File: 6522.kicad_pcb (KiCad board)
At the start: 2 copper layers, 65.8 x 81.4 mm, 20 parts, among them J1 Conn_02x20_Top_Bottom, J2 Conn_02x01_Top_Bottom, P1 A2Bus, U1 74LS245, U2 74LS04, U3 74LS74, U4 W65C22, U5 W65C22

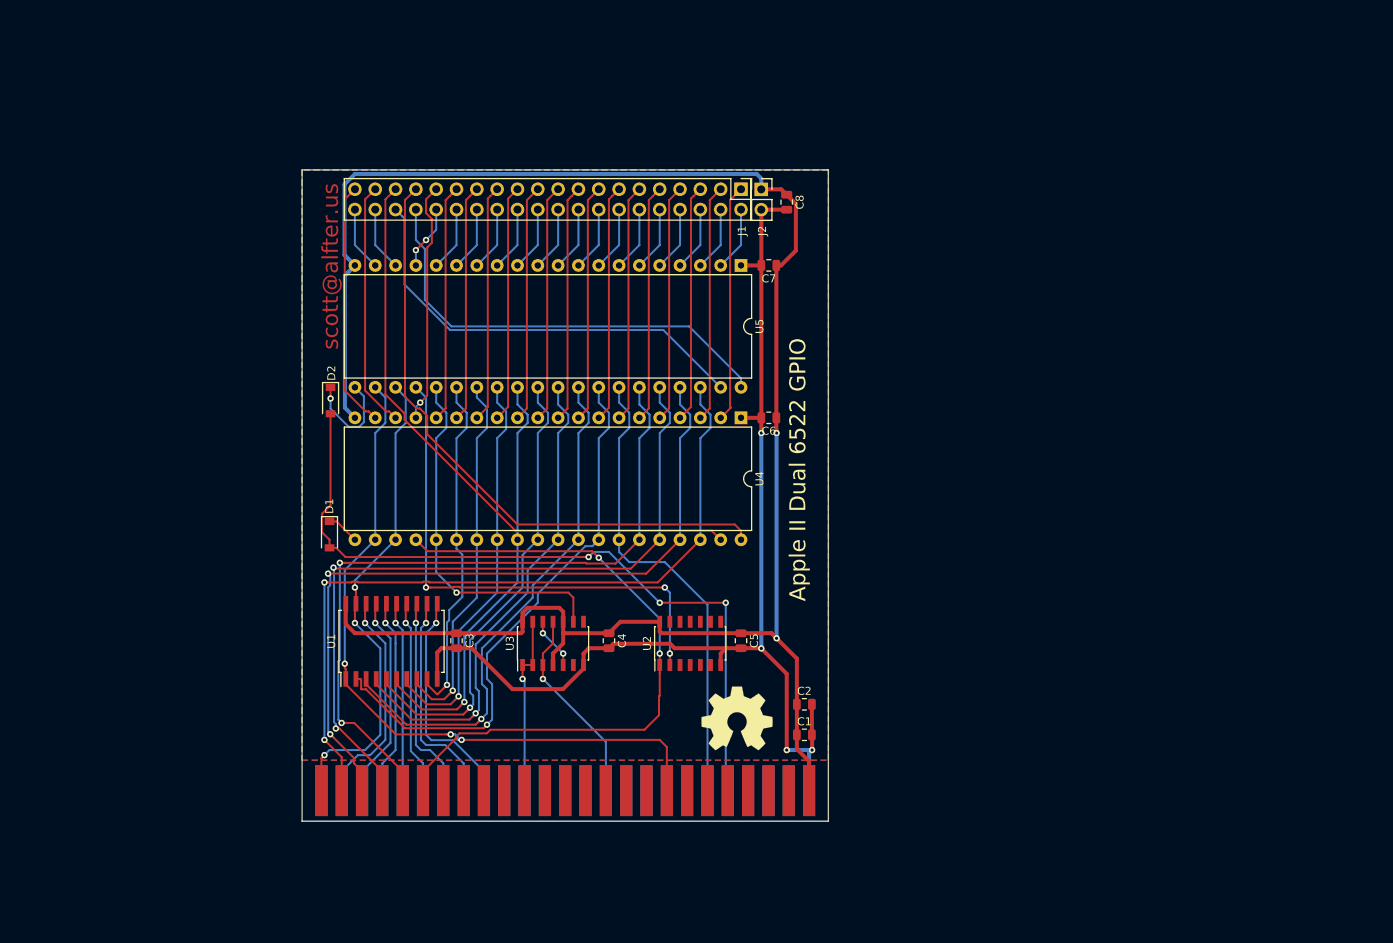
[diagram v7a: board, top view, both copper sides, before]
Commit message: Mockingboard with delay-based Phi2
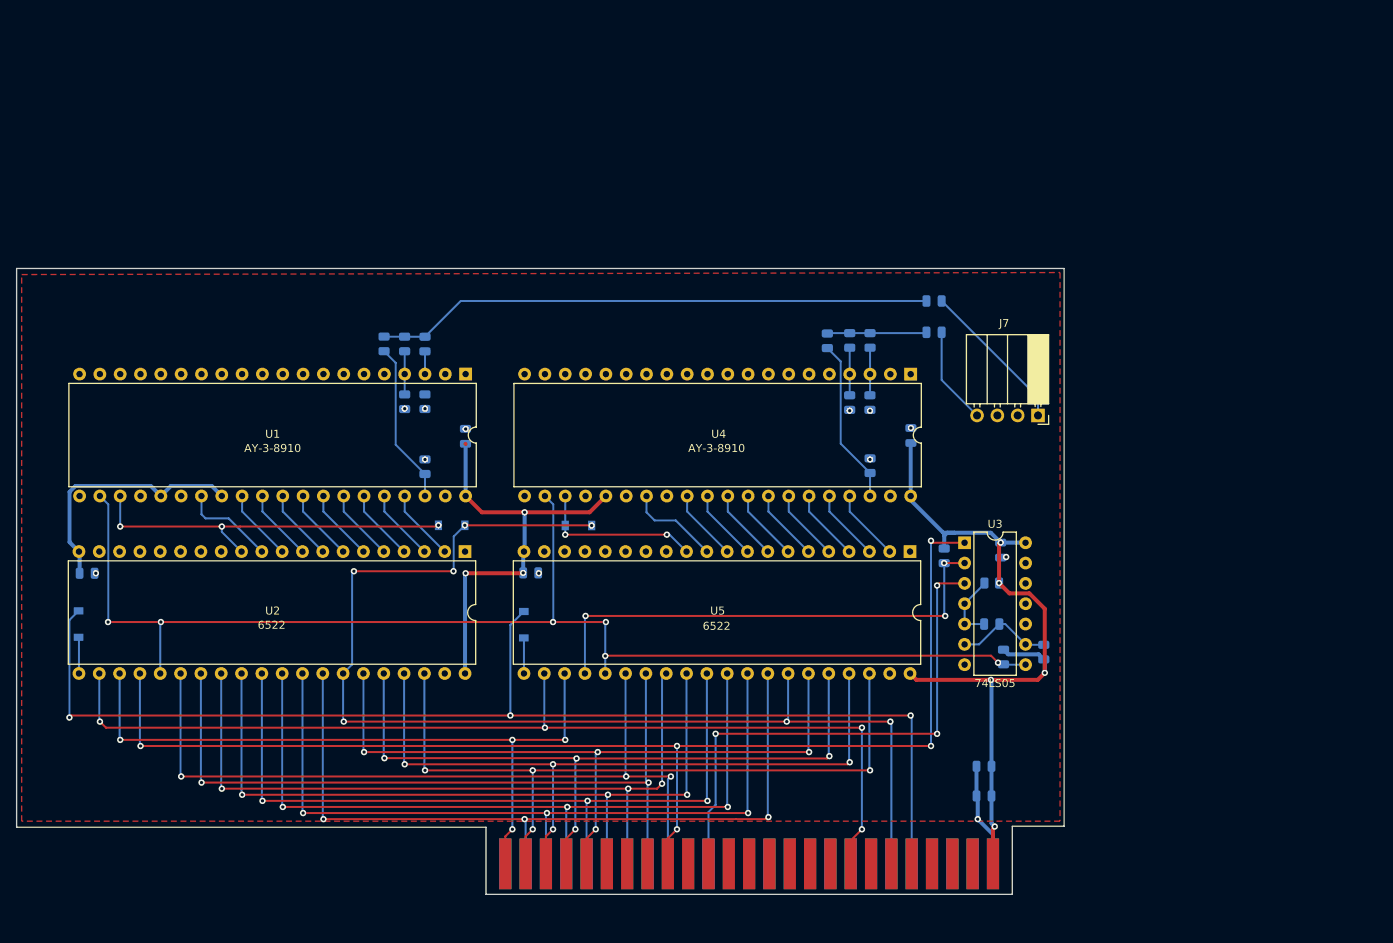
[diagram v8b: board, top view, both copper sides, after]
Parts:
- removed the C8 at (172.0, 56.7)
- removed G***: LOGO, qr:qr
- removed J1: Conn_02x20_Top_Bottom, Connector_PinHeader_2.54mm:PinHeader_2x20_P2.54mm_Vertical
- removed J2: Conn_02x01_Top_Bottom, Connector_PinHeader_2.54mm:PinHeader_2x01_P2.54mm_Vertical
- removed REF**: OSHW-Symbol_8.9x8mm_SilkScreen, Symbol:OSHW-Symbol_8.9x8mm_SilkScreen
- removed the U2 at (159.9, 111.9)
- added C1: 10μF, Capacitor_SMD:C_0805_2012Metric, B.Cu at (190.4, 69.1)
- added C10: 10μF, Capacitor_SMD:C_0805_2012Metric, B.Cu at (190.4, 73.0)
- added C9: 5pF, Capacitor_SMD:C_0805_2012Metric, B.Cu at (197.6, 109.5)
- added D1: BAT54GW, Diode_SMD:D_SOD-123, B.Cu at (130.1, 97.1)
- added D3: BAT54GW, Diode_SMD:D_SOD-123, B.Cu at (145.9, 97.2)
- added J7: AUDIO_OUT, Connector_PinSocket_2.54mm:PinSocket_1x04_P2.54mm_Horizontal, F.Cu at (203.4, 83.4)
- added R1: 1k, Resistor_SMD:R_0805_2012Metric, B.Cu at (124.2, 74.5)
- added R10: 1k0, Resistor_SMD:R_0805_2012Metric, B.Cu at (199.1, 113.6)
- added R11: 1k, Resistor_SMD:R_0805_2012Metric, B.Cu at (179.8, 74.0)
- added R12: 1k, Resistor_SMD:R_0805_2012Metric, B.Cu at (182.4, 74.0)
- added R13: 1k, Resistor_SMD:R_0805_2012Metric, B.Cu at (177.0, 74.1)
- added R14: 470, Resistor_SMD:R_0805_2012Metric, B.Cu at (179.8, 81.8)
- added R15: 470, Resistor_SMD:R_0805_2012Metric, B.Cu at (182.4, 81.8)
- added R16: 470, Resistor_SMD:R_0805_2012Metric, B.Cu at (182.4, 89.7)
- added R2: 1k, Resistor_SMD:R_0805_2012Metric, B.Cu at (126.7, 74.5)
- added R3: 1k, Resistor_SMD:R_0805_2012Metric, B.Cu at (121.6, 74.5)
- added R4: 470, Resistor_SMD:R_0805_2012Metric, B.Cu at (124.2, 81.7)
- added R5: 470, Resistor_SMD:R_0805_2012Metric, B.Cu at (126.7, 81.7)
- added R6: 470, Resistor_SMD:R_0805_2012Metric, B.Cu at (126.7, 89.8)
- added R7: 10k, Resistor_SMD:R_0805_2012Metric, B.Cu at (191.6, 100.9)
- added R8: 4k7, Resistor_SMD:R_0805_2012Metric, B.Cu at (197.6, 104.3)
- added R9: 4k7, Resistor_SMD:R_0805_2012Metric, B.Cu at (204.1, 113.0)
- added U4: AY-3-8910, Package_DIP:DIP-40_W15.24mm, F.Cu at (187.5, 78.2)
- C2: renamed from C1; moved to B.Cu
- C3: renamed from C2; moved to B.Cu
- C4: renamed from C3; moved to B.Cu
- C5: renamed from C4; moved to B.Cu
- C6: renamed from C5; moved to B.Cu
- C7: renamed from C6; moved to B.Cu
- C8: renamed from C7; moved to B.Cu
- D2: renamed from D1; moved to B.Cu
- D4: renamed from D2; moved to B.Cu
- U1: value 74LS245 -> AY-3-8910; footprint Package_SO:SOIC-20W_7.5x12.8mm_P1.27mm -> Package_DIP:DIP-40_W15.24mm
- U2: renamed from U4; value W65C22 -> 6522
- U3: value 74LS74 -> 74LS05; footprint Package_SO:SOIC-14_3.9x8.7mm_P1.27mm -> Package_DIP:DIP-14_W7.62mm
- U5: value W65C22 -> 6522
- moved C6 82.2 mm to (84.5, 103.1), turned to 0 degrees
- moved C8 71.6 mm to (196.6, 131.0)
- moved U3 53.0 mm to (194.2, 99.3), turned to 0 degrees
- moved C5 50.3 mm to (198.7, 100.2)
- moved U5 41.5 mm to (187.4, 100.4)
- moved U2 38.3 mm to (131.7, 100.4)
- moved C7 38.0 mm to (131.8, 86.0), turned to 90 degrees
- moved D4 37.0 mm to (139.1, 109.6), turned to 90 degrees
- moved C3 36.1 mm to (187.5, 85.9), turned to 90 degrees
- moved U1 34.7 mm to (131.8, 78.2), turned to -90 degrees
- moved D2 33.3 mm to (83.4, 109.5), turned to 90 degrees
- moved P1 24.7 mm to (167.3, 139.4)
- moved C2 22.8 mm to (196.6, 127.3), turned to 180 degrees
- moved C4 12.6 mm to (140.0, 103.1), turned to 0 degrees
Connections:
- net ~IRQ renamed ~{IRQ}
- net ~RES renamed ~{RES}
- P1 pad 1: ~IOSEL -> ~{IOSEL}
- P1 pad 10: Net-(P1-Pad10) -> unconnected-(P1-Pad10)
- P1 pad 11: Net-(P1-Pad11) -> unconnected-(P1-Pad11)
- P1 pad 12: Net-(P1-Pad12) -> unconnected-(P1-Pad12)
- P1 pad 13: Net-(P1-Pad13) -> unconnected-(P1-Pad13)
- P1 pad 14: Net-(P1-Pad14) -> unconnected-(P1-Pad14)
- P1 pad 15: Net-(P1-Pad15) -> unconnected-(P1-Pad15)
- P1 pad 16: Net-(P1-Pad16) -> unconnected-(P1-Pad16)
- P1 pad 17: Net-(P1-Pad17) -> unconnected-(P1-Pad17)
- P1 pad 18: R~W -> R~{W}
- P1 pad 19: Net-(P1-Pad19) -> unconnected-(P1-Pad19)
- P1 pad 20: Net-(P1-Pad20) -> unconnected-(P1-Pad20)
- P1 pad 21: Net-(P1-Pad21) -> unconnected-(P1-Pad21)
- P1 pad 22: Net-(P1-Pad22) -> unconnected-(P1-Pad22)
- P1 pad 27: Net-(P1-Pad27) -> Net-(P1-Pad24)
- P1 pad 28: Net-(P1-Pad28) -> Net-(P1-Pad23)
- P1 pad 29: Net-(P1-Pad29) -> unconnected-(P1-Pad29)
- P1 pad 32: Net-(P1-Pad32) -> unconnected-(P1-Pad32)
- P1 pad 33: Net-(P1-Pad33) -> unconnected-(P1-Pad33)
- P1 pad 34: Net-(P1-Pad34) -> unconnected-(P1-Pad34)
- P1 pad 35: Net-(P1-Pad35) -> unconnected-(P1-Pad35)
- P1 pad 36: 7M -> unconnected-(P1-Pad36)
- P1 pad 37: Net-(P1-Pad37) -> unconnected-(P1-Pad37)
- P1 pad 38: Net-(P1-Pad38) -> unconnected-(P1-Pad38)
- P1 pad 39: Net-(P1-Pad39) -> unconnected-(P1-Pad39)
- P1 pad 41: Net-(P1-Pad41) -> unconnected-(P1-Pad41)
- P1 pad 42: Net-(P1-Pad42) -> D7
- P1 pad 43: Net-(P1-Pad43) -> D6
- P1 pad 44: Net-(P1-Pad44) -> D5
- P1 pad 45: Net-(P1-Pad45) -> D4
- P1 pad 46: Net-(P1-Pad46) -> D3
- P1 pad 47: Net-(P1-Pad47) -> D2
- P1 pad 48: Net-(P1-Pad48) -> D1
- P1 pad 49: Net-(P1-Pad49) -> D0
- P1 pad 50: Net-(P1-Pad50) -> unconnected-(P1-Pad50)
- P1 pad 6: A4 -> unconnected-(P1-Pad6)
- P1 pad 7: Net-(P1-Pad7) -> unconnected-(P1-Pad7)
- P1 pad 8: Net-(P1-Pad8) -> unconnected-(P1-Pad8)
- P1 pad 9: Net-(P1-Pad9) -> A7
- U1 pad 1: R~W -> GND
- U1 pad 10: GND -> unconnected-(U1-Pad10)
- U1 pad 11: Net-(P1-Pad42) -> unconnected-(U1-Pad11)
- U1 pad 12: Net-(P1-Pad43) -> unconnected-(U1-Pad12)
- U1 pad 13: Net-(P1-Pad44) -> unconnected-(U1-Pad13)
- U1 pad 14: Net-(P1-Pad45) -> unconnected-(U1-Pad14)
- U1 pad 15: Net-(P1-Pad46) -> unconnected-(U1-Pad15)
- U1 pad 16: Net-(P1-Pad47) -> unconnected-(U1-Pad16)
- U1 pad 17: Net-(P1-Pad48) -> unconnected-(U1-Pad17)
- U1 pad 18: Net-(P1-Pad49) -> unconnected-(U1-Pad18)
- U1 pad 19: ~IOSEL -> unconnected-(U1-Pad19)
- U1 pad 2: D0 -> unconnected-(U1-Pad2)
- U1 pad 20: VCC -> unconnected-(U1-Pad20)
- U1 pad 3: D1 -> Net-(R2-Pad1)
- U1 pad 4: D2 -> Net-(R1-Pad1)
- U1 pad 5: D3 -> unconnected-(U1-Pad5)
- U1 pad 6: D4 -> unconnected-(U1-Pad6)
- U1 pad 7: D5 -> unconnected-(U1-Pad7)
- U1 pad 8: D6 -> unconnected-(U1-Pad8)
- U1 pad 9: D7 -> unconnected-(U1-Pad9)
- U2 pad 13: PB3 -> unconnected-(U2-Pad13)
- U2 pad 14: PB4 -> unconnected-(U2-Pad14)
- U2 pad 15: PB5 -> unconnected-(U2-Pad15)
- U2 pad 16: PB6 -> unconnected-(U2-Pad16)
- U2 pad 17: PB7 -> unconnected-(U2-Pad17)
- U2 pad 18: CB1 -> unconnected-(U2-Pad18)
- U2 pad 19: CB2 -> unconnected-(U2-Pad19)
- U2 pad 2: PA0 -> Net-(U1-Pad37)
- U2 pad 22: R~W -> R~{W}
- U2 pad 23: ~IOSEL -> ~{IOSEL}
- U2 pad 24: A4 -> A7
- U2 pad 3: PA1 -> Net-(U1-Pad36)
- U2 pad 39: CA2 -> unconnected-(U2-Pad39)
- U2 pad 4: PA2 -> Net-(U1-Pad35)
- U2 pad 40: CA1 -> VCC
- U2 pad 5: PA3 -> Net-(U1-Pad34)
- U2 pad 6: PA4 -> Net-(U1-Pad33)
- U2 pad 7: PA5 -> Net-(U1-Pad32)
- U2 pad 8: PA6 -> Net-(U1-Pad31)
- U2 pad 9: PA7 -> Net-(U1-Pad30)
- U3 pad 1: PHI0 -> A7
- U3 pad 10: VCC -> (no net)
- U3 pad 11: 7M -> (no net)
- U3 pad 12: Net-(U3-Pad12) -> (no net)
- U3 pad 13: PHI0 -> (no net)
- U3 pad 2: PHI0 -> Net-(R7-Pad1)
- U3 pad 3: 7M -> PHI0
- U3 pad 4: VCC -> Net-(C9-Pad2)
- U3 pad 5: Net-(U3-Pad12) -> Net-(C9-Pad2)
- U3 pad 6: Net-(U3-Pad6) -> Net-(C9-Pad1)
- U3 pad 8: Net-(U3-Pad8) -> PHI2
- U3 pad 9: PHI2 -> Net-(C9-Pad1)
- U5 pad 13: PD3 -> unconnected-(U5-Pad13)
- U5 pad 14: PD4 -> unconnected-(U5-Pad14)
- U5 pad 15: PD5 -> unconnected-(U5-Pad15)
- U5 pad 16: PD6 -> unconnected-(U5-Pad16)
- U5 pad 17: PD7 -> unconnected-(U5-Pad17)
- U5 pad 18: CD1 -> unconnected-(U5-Pad18)
- U5 pad 19: CD2 -> unconnected-(U5-Pad19)
- U5 pad 2: PC0 -> Net-(U4-Pad37)
- U5 pad 22: R~W -> R~{W}
- U5 pad 23: ~IOSEL -> ~{IOSEL}
- U5 pad 24: Net-(U2-Pad2) -> Net-(R7-Pad1)
- U5 pad 3: PC1 -> Net-(U4-Pad36)
- U5 pad 39: CC2 -> unconnected-(U5-Pad39)
- U5 pad 4: PC2 -> Net-(U4-Pad35)
- U5 pad 40: CC1 -> VCC
- U5 pad 5: PC3 -> Net-(U4-Pad34)
- U5 pad 6: PC4 -> Net-(U4-Pad33)
- U5 pad 7: PC5 -> Net-(U4-Pad32)
- U5 pad 8: PC6 -> Net-(U4-Pad31)
- U5 pad 9: PC7 -> Net-(U4-Pad30)
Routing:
- net A7: track 0.00 -> 153.1 mm, vias 0 -> 5
- net GND: track 145.4 -> 14.6 mm, vias 4 -> 12
- net R~{W}: track 0.00 -> 126.0 mm, vias 0 -> 4
- net PHI2: track 45.6 -> 160.6 mm, vias 1 -> 6
- net R~W: track 90.8 -> 0.00 mm, vias 3 -> 0
- net ~{IOSEL}: track 0.00 -> 88.2 mm, vias 0 -> 4
- net ~{RES}: track 60.6 -> 146.3 mm, vias 0 -> 7
- net A4: track 83.5 -> 0.00 mm, vias 2 -> 0
- net CA1: track 77.9 -> 0.00 mm
- net CA2: track 76.1 -> 0.00 mm
- net Net-(C1-Pad1): track 0.00 -> 69.7 mm
- net Net-(U2-Pad2): track 65.4 -> 0.00 mm, vias 3 -> 0
- net ~IOSEL: track 62.6 -> 0.00 mm, vias 3 -> 0
- net Net-(R7-Pad1): track 0.00 -> 61.4 mm, vias 0 -> 3
- net VCC: track 237.5 -> 179.8 mm, vias 2 -> 8
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- added copper zone on F.Cu, net GND
- removed copper zone on B.Cu, net (none)
- removed copper zone on F.Cu, net (none)
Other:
- board size 65.8 x 81.4 mm -> 130.9 x 78.2 mm
- net class Default removed
- net class Power removed
- board text removed: "Apple II Dual 6522 GPIO"
- board text removed: "https://gitlab.com/salfter/a2gpio"
- board text removed: "scott@alfter.us"
